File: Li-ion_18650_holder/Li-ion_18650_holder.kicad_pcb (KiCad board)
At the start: 2 copper layers, 81.3 x 17.8 mm, 14 parts, among them J1 P+, J2 P+, J3 P+, J4 P-, J5 P-, J6 P-, Q1 IRLR8726, Q2 IRLR8726, SW1 SW_Push, U1 AP9101CAK6-ANTRG1

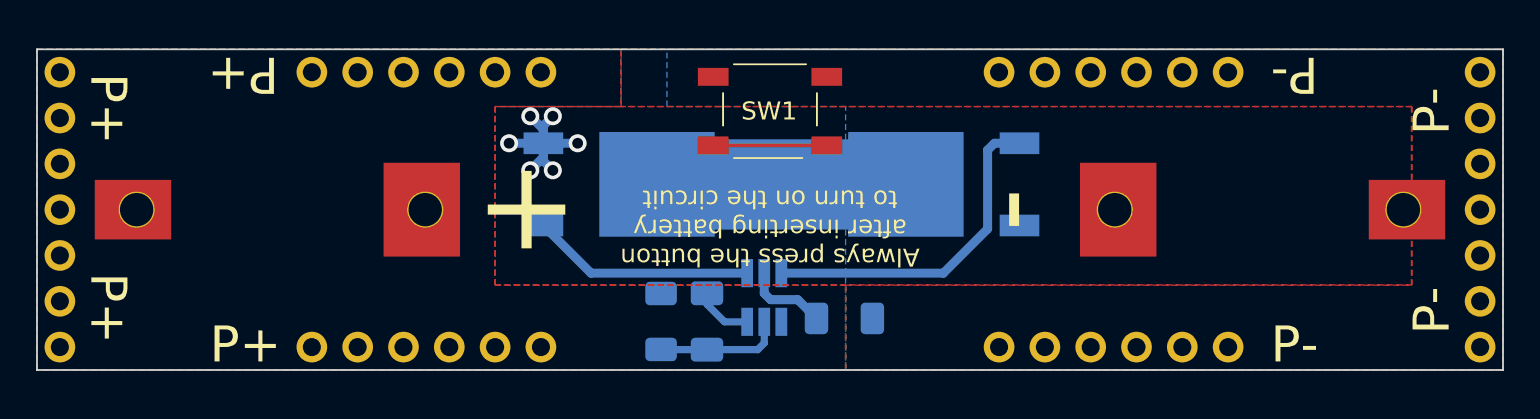
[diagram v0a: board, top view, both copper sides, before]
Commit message: Added stitching between pours and pulled copper back from edges
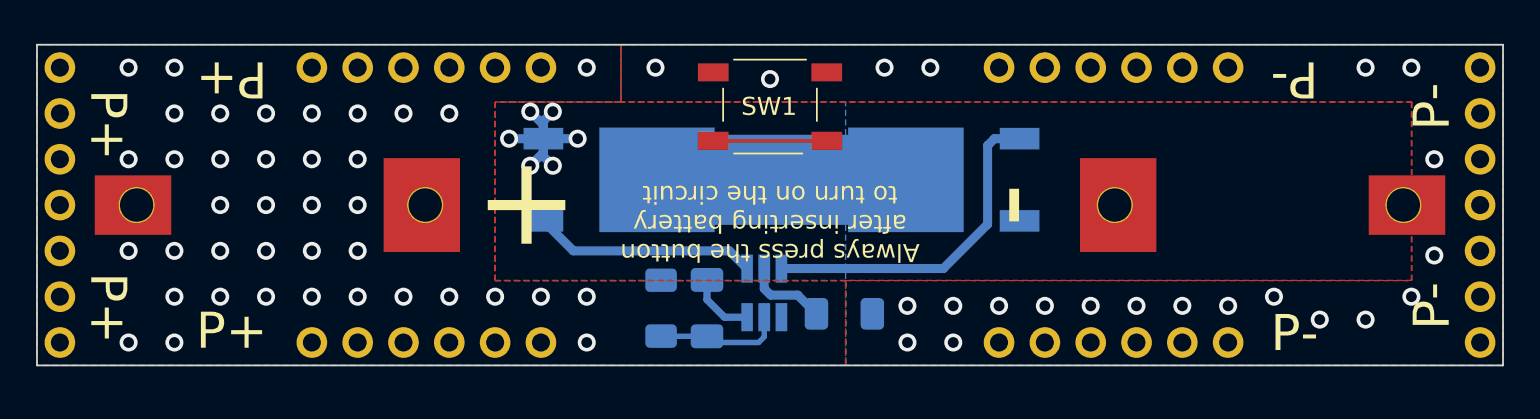
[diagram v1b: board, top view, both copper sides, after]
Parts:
- moved C1 0.74 mm to (138.7, 104.8)
- moved R1 0.74 mm to (136.2, 104.8)
- moved J3 0.25 mm to (123.2, 91.4)
- moved J6 0.25 mm to (161.3, 91.4)
- moved Q1 0.25 mm to (133.9, 97.7)
- moved Q2 0.25 mm to (151.9, 97.7)
- moved BT1 0.25 mm to (142.2, 99.1)
- moved J1 0.25 mm to (123.2, 106.7)
- moved J2 0.25 mm to (102.9, 99.1)
- moved J4 0.25 mm to (161.3, 106.7)
- moved J5 0.25 mm to (181.6, 99.1)
- moved R2 0.25 mm to (146.4, 105.1)
- moved SW1 0.25 mm to (142.2, 93.6)
- moved U1 0.25 mm to (141.9, 103.9)
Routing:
- net Net-(BT1-Pad1): vias 0 -> 39
- net GND: vias 0 -> 22
